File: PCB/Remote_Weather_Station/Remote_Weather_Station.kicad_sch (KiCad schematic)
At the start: 25 parts, among them J101 strain_gauge_N, J102 strain_gauge_E, J103 strain_gauge_S, J104 strain_gauge_W, J105 load_cell_in, J106 UART, J107 Stemma_QT_Connector, J108 Servo_Connector, SW101 SW_Push, SW102 SW_Push, U101 ESP32-WROOM-32D

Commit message: Add files via upload
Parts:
- removed J105: load_cell_in, symbol Connector_Generic:Conn_01x02
- added C104, C106, C107: 1uF, symbol Device:C_Small
- added J109: load_cell_in, symbol Connector_Generic:Conn_01x04
- added R106, R109, R112: Rg, symbol Device:R_Small_US
- added R107, R110, R117: 11k, symbol Device:R_Small_US
- added R108, R111, R118: 4.7k, symbol Device:R_Small_US
- added U102, U103, U104: AD8227, symbol Amplifier_Instrumentation:AD8236
- R101, R104: value 350 -> 20
- R102, R103: value 350 -> 330
- R105, R116: value 12k -> 4.7k
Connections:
- net +3.3V: now also J101.1 (Pin_1), J102.1 (Pin_1), R101.2, C104.1, C106.2, C107.2, J109.4 (Pin_4); no longer R101.1, R102.1, R103.1, R104.1
- net +5V: now also R107.1, R110.1, R117.1, U102.8 (Vs+), U103.8 (Vs+), U104.8 (Vs+)
- net GND: now also R102.1, C104.2, C106.1, C107.1, J109.1 (Pin_1), R108.2, R111.2, R118.2, U102.5 (Vs-), U103.5 (Vs-), U104.5 (Vs-); no longer J101.2 (Pin_2), J102.2 (Pin_2)
- net Green_Wire: now also J109.3 (Pin_3), U104.1 (-)
- net Servo: now also U101.30 (IO18); no longer U101.37 (IO23)
- net White_Wire: now also J109.2 (Pin_2), U104.4 (+)
- removed net East_Test: J102.1 (Pin_1), R102.2, U101.16 (IO13)
- removed net North_Test: J101.1 (Pin_1), R101.2, U101.14 (IO12)
- removed net South_Test: J103.1 (Pin_1), R103.2, U101.13 (IO14)
- net Vwater: no longer names the net of U101.27 (IO16)
- removed net West_Test: J104.1 (Pin_1), R104.2, U101.23 (IO15)
- new net: R101.1, R103.2
- new net: R110.2, R111.1, U103.6 (Ref)
- new net: R107.2, R108.1, U102.6 (Ref)
- new net: R106.1, U102.2 (Rg)
- new net: R106.2, U102.3 (Rg)
- new net: R109.1, U103.2 (Rg)
- new net: R109.2, U103.3 (Rg)
- new net: R117.2, R118.1, U104.6 (Ref)
- new net: R112.1, U104.2 (Rg)
- new net: R112.2, U104.3 (Rg)
- new net: R102.2, R104.1
- new net Base_Ref: R103.1, R104.2, U102.1 (-), U103.1 (-)
- new net E_W_Value: U101.16 (IO13), U103.7
- new net East_West_Ref: J102.2 (Pin_2), J104.1 (Pin_1), U103.4 (+)
- new net N_S_Value: U101.14 (IO12), U102.7
- new net North_South_Ref: J101.2 (Pin_2), J103.1 (Pin_1), U102.4 (+)
- new net Rain_Value: U101.13 (IO14), U104.7
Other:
- added sheet PDN (PDN.kicad_sch)
- note added: "Instrumentation Amps"
- note added: "PDN"
- note removed: "Instrumentation Amplifier Setup"
- moved on the sheet: J101, J103

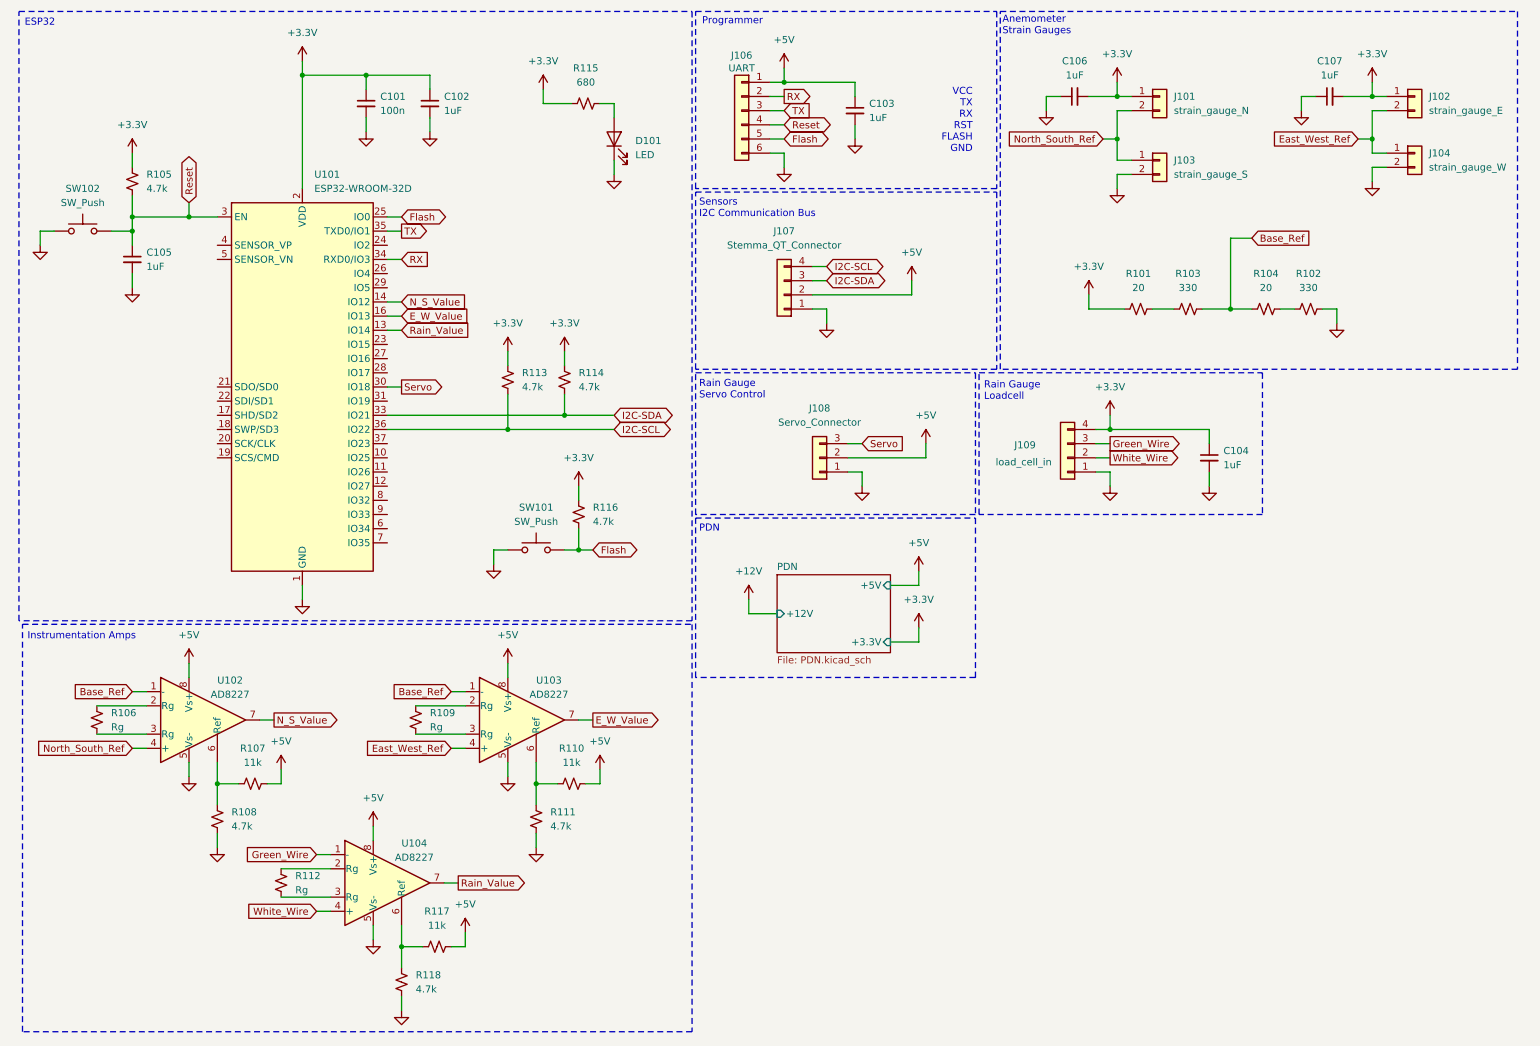
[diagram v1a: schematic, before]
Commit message: Add files via upload
Added input caps to PDN
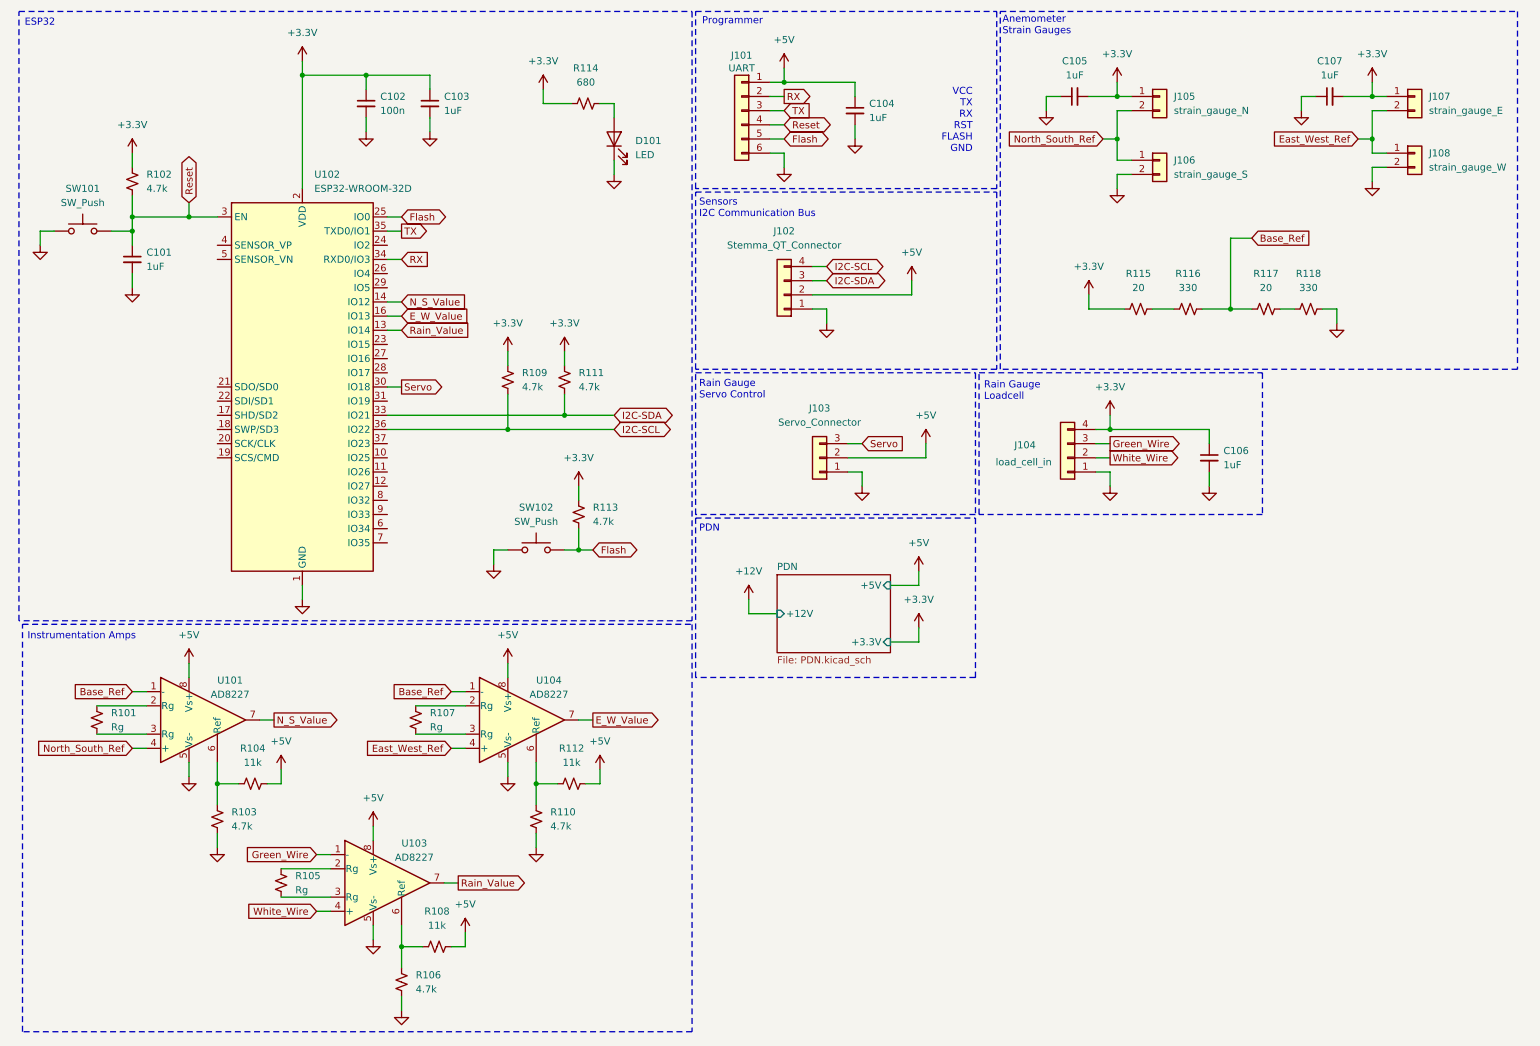
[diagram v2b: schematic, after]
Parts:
- renumbered C105 to C101, C101 to C102, C102 to C103, C103 to C104, C106 to C105, C104 to C106, J106 to J101, J107 to J102, J108 to J103, J109 to J104, J101 to J105, J103 to J106, J102 to J107, J104 to J108, R106 to R101, R105 to R102, R108 to R103, R107 to R104, R112 to R105, R118 to R106, R109 to R107, R117 to R108, R113 to R109, R111 to R110, R114 to R111, R110 to R112, R116 to R113, R115 to R114, R101 to R115, R103 to R116, R104 to R117, R102 to R118, SW102 to SW101, SW101 to SW102, U102 to U101, U101 to U102, U104 to U103, U103 to U104

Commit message: Add files via upload
Added footprints and JLC numbers for some of the parts. Still lacking a few on the higher level but should be able to start PCB stuff for PDN now!
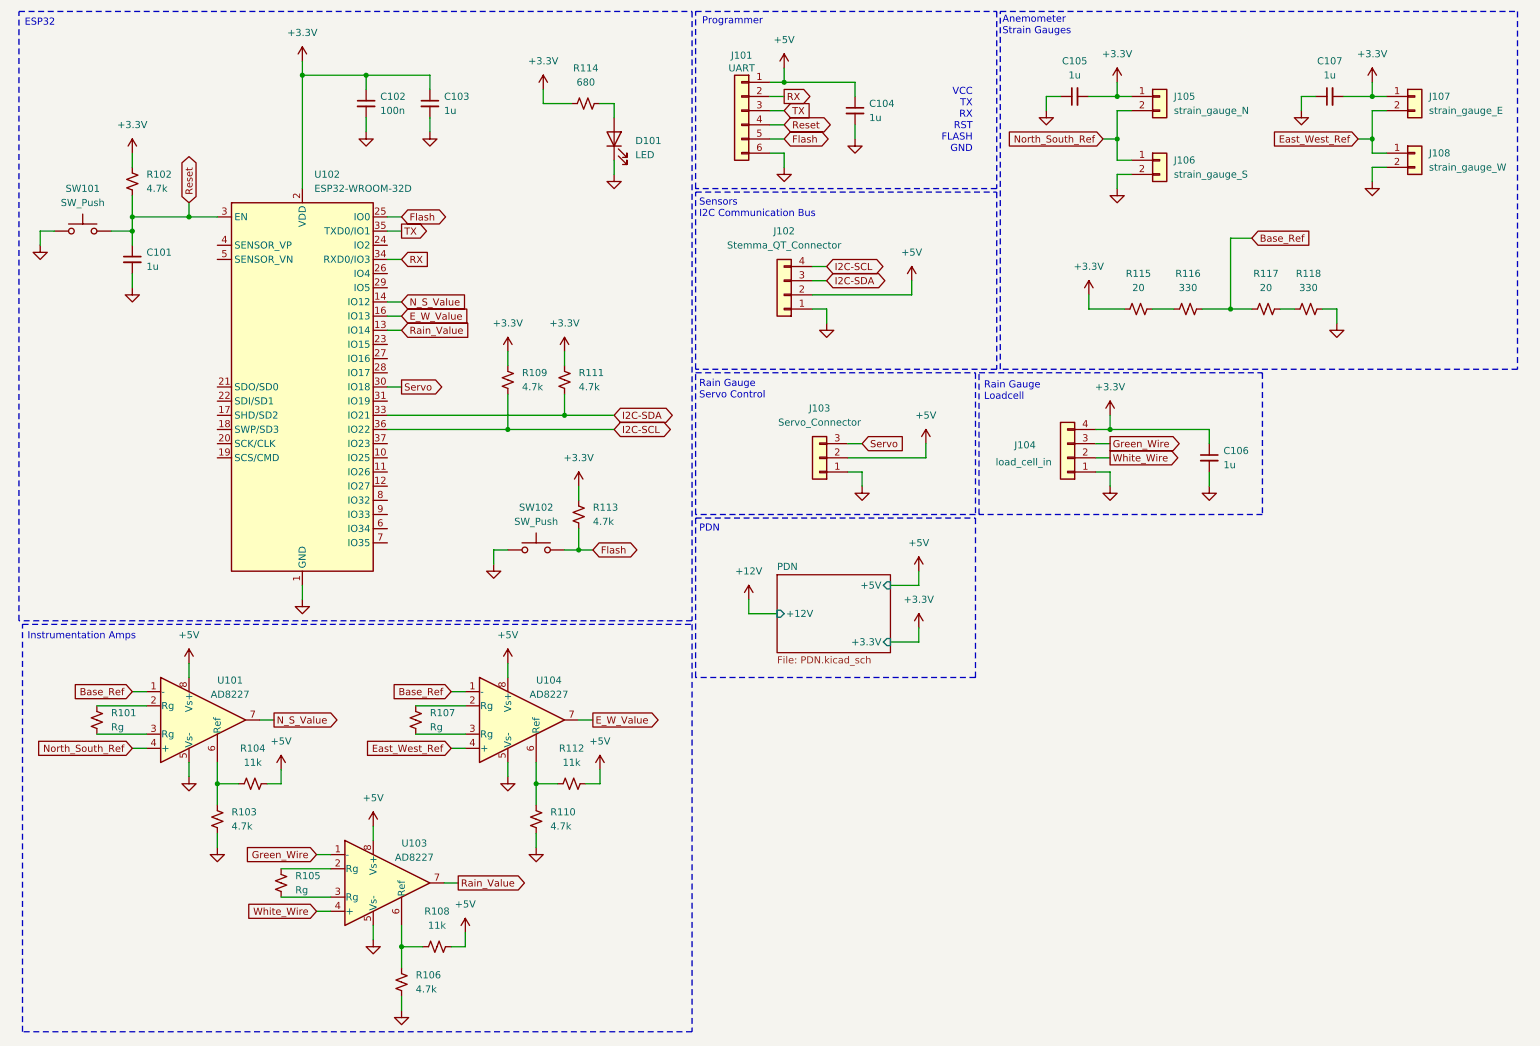
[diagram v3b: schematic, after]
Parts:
- C101, C103, C104, C105, C106, C107: value 1uF -> 1u; footprint (none) -> Capacitor_SMD:C_0805_2012Metric; JLCPCB# (none) -> C28323
- C102: footprint (none) -> Capacitor_SMD:C_0805_2012Metric; JLCPCB# (none) -> C49678
- R101, R102, R103, R104, R105, R106, R107, R108, R109, R110, R111, R112, R113, R114, R115, R116, R117, R118: footprint (none) -> Resistor_SMD:R_0402_1005Metric
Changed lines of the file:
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@@
 			)
 		)
-		(property "Value" "1uF"
+		(property "Value" "1u"
 			(at 36.83 59.6962 0)
 			(effects
@@
 			)
 		)
-		(property "Footprint" ""
+		(property "Footprint" "Capacitor_SMD:C_0805_2012Metric"
 			(at 34.29 58.42 0)
 			(effects
@@
 			)
 		)
+		(property "JLCPCB#" "C28323"
+			(at 34.29 58.42 0)
+			(effects
+				(font
+					(size 1.27 1.27)
+				)
+				(hide yes)
+			)
+		)
 		(pin "2"
 		)
@@
 			)
 		)
-		(property "Footprint" ""
+		(property "Footprint" "Resistor_SMD:R_0402_1005Metric"
 			(at 214.63 67.31 0)
 			(effects
@@
 			)
 		)
-		(property "Footprint" ""
+		(property "Footprint" "Resistor_SMD:R_0402_1005Metric"
 			(at 106.68 158.75 0)
 			(effects
@@
 			)
 		)
-		(property "Footprint" ""
+		(property "Footprint" "Resistor_SMD:R_0402_1005Metric"
 			(at 55.88 152.4 0)
 			(effects
@@
 			)
 		)
-		(property "Footprint" ""
+		(property "Footprint" "Resistor_SMD:R_0402_1005Metric"
 			(at 27.94 140.97 0)
 			(effects
@@
 			)
 		)
-		(property "Footprint" ""
+		(property "Footprint" "Resistor_SMD:R_0402_1005Metric"
 			(at 85.09 140.97 0)
 			(effects
@@
 			)
 		)
-		(property "Footprint" ""
+		(property "Footprint" "Capacitor_SMD:C_0805_2012Metric"
 			(at 76.2 30.48 0)
 			(effects
@@
 			)
 		)
+		(property "JLCPCB#" "C49678"
+			(at 76.2 30.48 0)
+			(effects
+				(font
+					(size 1.27 1.27)
+				)
+				(hide yes)
+			)
+		)
 		(pin "2"
 		)
@@
 			)
 		)
-		(property "Footprint" ""
+		(property "Footprint" "Resistor_SMD:R_0402_1005Metric"
 			(at 223.52 67.31 0)
 			(effects
@@
 			)
 		)
-		(property "Value" "1uF"
+		(property "Value" "1u"
 			(at 248.9263 25.4 90)
 			(effects
@@
 			)
 		)
-		(property "Footprint" ""
+		(property "Footprint" "Capacitor_SMD:C_0805_2012Metric"
 			(at 248.92 29.21 0)
 			(effects
@@
 			)
 		)
-		(property "JLCPCB#" ""
+		(property "JLCPCB#" "C28323"
 			(at 248.92 29.21 0)
 			(effects
@@
 			)
 		)
-		(property "Footprint" ""
+		(property "Footprint" "Resistor_SMD:R_0402_1005Metric"
 			(at 88.9 181.61 0)
 			(effects
@@
 			)
 		)
-		(property "Footprint" ""
+		(property "Footprint" "Resistor_SMD:R_0402_1005Metric"
 			(at 114.3 104.14 0)
 			(effects
@@
 			)
 		)
-		(property "Footprint" ""
+		(property "Footprint" "Resistor_SMD:R_0402_1005Metric"
 			(at 115.57 30.48 0)
 			(effects
@@
 			)
 		)
+		(property "JLCPCB#" ""
+			(at 115.57 30.48 0)
+			(effects
+				(font
+					(size 1.27 1.27)
+				)
+				(hide yes)
+			)
+		)
 		(pin "2"
 		)
@@
 			)
 		)
-		(property "Footprint" ""
+		(property "Footprint" "Resistor_SMD:R_0402_1005Metric"
 			(at 60.96 170.18 0)
 			(effects
@@
 			)
 		)
-		(property "Value" "1uF"
+		(property "Value" "1u"
 			(at 166.37 33.0262 0)
 			(effects
@@
 			)
 		)
-		(property "Footprint" ""
+		(property "Footprint" "Capacitor_SMD:C_0805_2012Metric"
 			(at 163.83 31.75 0)
 			(effects
@@
 			)
 		)
+		(property "JLCPCB#" "C28323"
+			(at 163.83 31.75 0)
+			(effects
+				(font
+					(size 1.27 1.27)
+				)
+				(hide yes)
+			)
+		)
 		(pin "2"
 		)
@@
 			)
 		)
-		(property "Footprint" ""
+		(property "Footprint" "Resistor_SMD:R_0402_1005Metric"
 			(at 34.29 44.45 0)
 			(effects
@@
 			)
 		)
-		(property "Value" "1uF"
+		(property "Value" "1u"
 			(at 203.2063 25.4 90)
 			(effects
@@
 			)
 		)
-		(property "Footprint" ""
+		(property "Footprint" "Capacitor_SMD:C_0805_2012Metric"
 			(at 203.2 29.21 0)
 			(effects
@@
 			)
 		)
-		(property "JLCPCB#" ""
+		(property "JLCPCB#" "C28323"
 			(at 203.2 29.21 0)
 			(effects
@@
 			)
 		)
-		(property "Footprint" ""
+		(property "Footprint" "Resistor_SMD:R_0402_1005Metric"
 			(at 101.6 80.01 0)
 			(effects
@@
 			)
 		)
-		(property "Footprint" ""
+		(property "Footprint" "Resistor_SMD:R_0402_1005Metric"
 			(at 82.55 187.96 0)
 			(effects
@@
 			)
 		)
-		(property "Value" "1uF"
+		(property "Value" "1u"
 			(at 90.17 31.7562 0)
 			(effects
@@
 			)
 		)
-		(property "Footprint" ""
+		(property "Footprint" "Capacitor_SMD:C_0805_2012Metric"
 			(at 87.63 30.48 0)
 			(effects
@@
 			)
 		)
+		(property "JLCPCB#" "C28323"
+			(at 87.63 30.48 0)
+			(effects
+				(font
+					(size 1.27 1.27)
+				)
+				(hide yes)
+			)
+		)
 		(pin "2"
 		)
@@
 			)
 		)
-		(property "Footprint" ""
+		(property "Footprint" "Resistor_SMD:R_0402_1005Metric"
 			(at 245.11 67.31 0)
 			(effects
@@
 			)
 		)
-		(property "Footprint" ""
+		(property "Footprint" "Resistor_SMD:R_0402_1005Metric"
 			(at 237.49 67.31 0)
 			(effects
@@
 			)
 		)
-		(property "Value" "1uF"
+		(property "Value" "1u"
 			(at 229.87 95.2562 0)
 			(effects
@@
 			)
 		)
-		(property "Footprint" ""
+		(property "Footprint" "Capacitor_SMD:C_0805_2012Metric"
 			(at 227.33 93.98 0)
 			(effects
@@
 			)
 		)
-		(property "JLCPCB#" ""
+		(property "JLCPCB#" "C28323"
 			(at 227.33 93.98 0)
 			(effects
@@
 			)
 		)
-		(property "Footprint" ""
+		(property "Footprint" "Resistor_SMD:R_0402_1005Metric"
 			(at 113.03 152.4 0)
 			(effects
@@
 			)
 		)
-		(property "Footprint" ""
+		(property "Footprint" "Resistor_SMD:R_0402_1005Metric"
 			(at 49.53 158.75 0)
 			(effects
@@
 			)
 		)
-		(property "Footprint" ""
+		(property "Footprint" "Resistor_SMD:R_0402_1005Metric"
 			(at 111.76 80.01 0)
 			(effects
